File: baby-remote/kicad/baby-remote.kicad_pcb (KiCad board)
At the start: 2 copper layers, 80 x 102 mm, 17 parts, among them SW1 Breast, SW10 Poop, SW11 Both, SW12 Change, SW13 Tummy, SW14 Weight, SW15 Note, SW2 Bottle, SW3 Solid, SW4 Sleep, SW5 PumpL, SW6 PumpR, SW7 Bath, SW8 Meds, SW9 Pee, U1 ESP32-C3 SuperMini

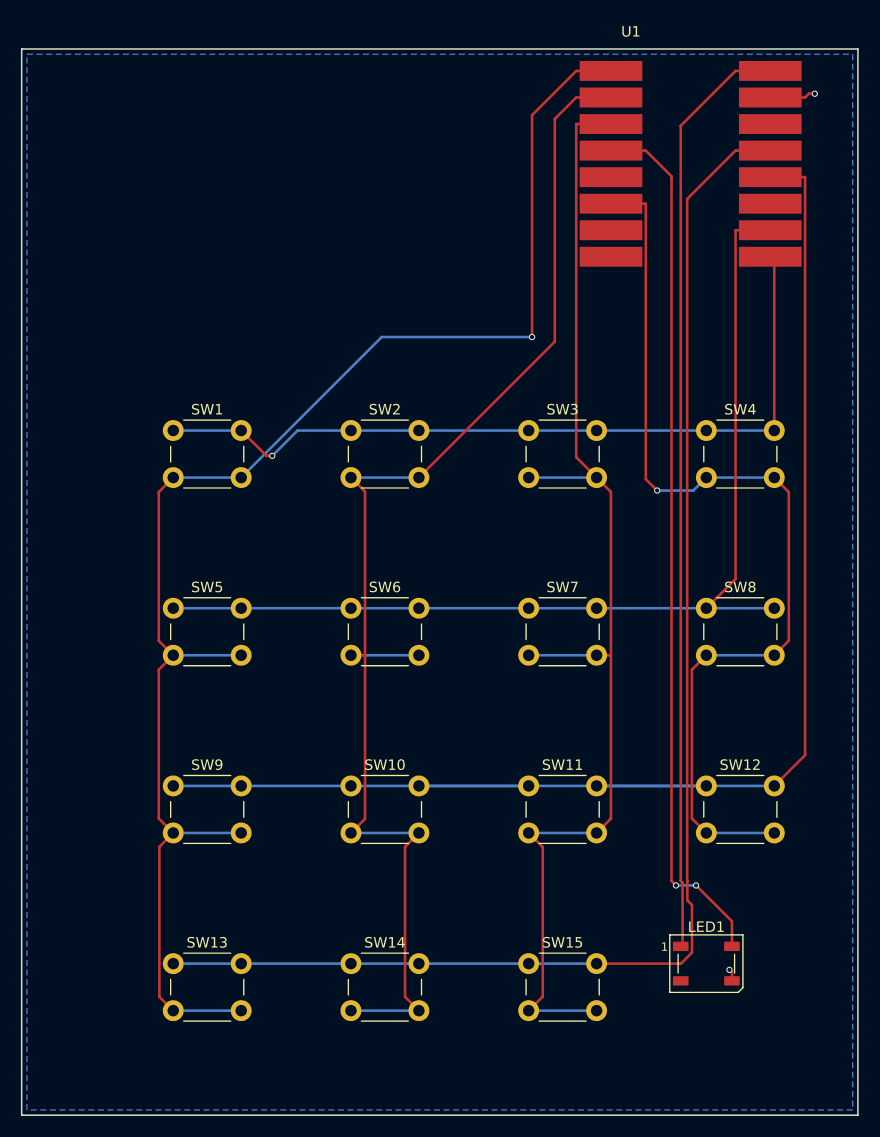
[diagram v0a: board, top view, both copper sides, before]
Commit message: feat(baby-remote): JLCPCB fab package + PCB-carrier enclosure + reserve page
- PCB trimmed to 80x100mm (bottom margin) to hit JLCPCB's <=100x100 5-pc tier;
  DRC still 0/0/0. Gerbers + drill exported to baby-remote/kicad/fab/ (JLCPCB zip).
- Enclosure reworked as a PCB carrier for the manufactured board: 80x100 board
  on a perimeter ledge, snap-fit cover, plunger-in-barrel barrels now hang from
  the cover over board-mounted switches, USB-C opening at the C3 port. STLs
  regenerated. v1 is USB-powered (LiPo deferred to v2).
- README: link the Baby Tracker App (hms-homelab/hms-baby-tracker), fix the STL
  table, add a "Want one?" reserve callout. RESERVE.md points at the
  shmaestro.com waitlist (build-on-demand).

Co-Authored-By: Claude Opus 4.8 (1M context) <noreply@anthropic.com>
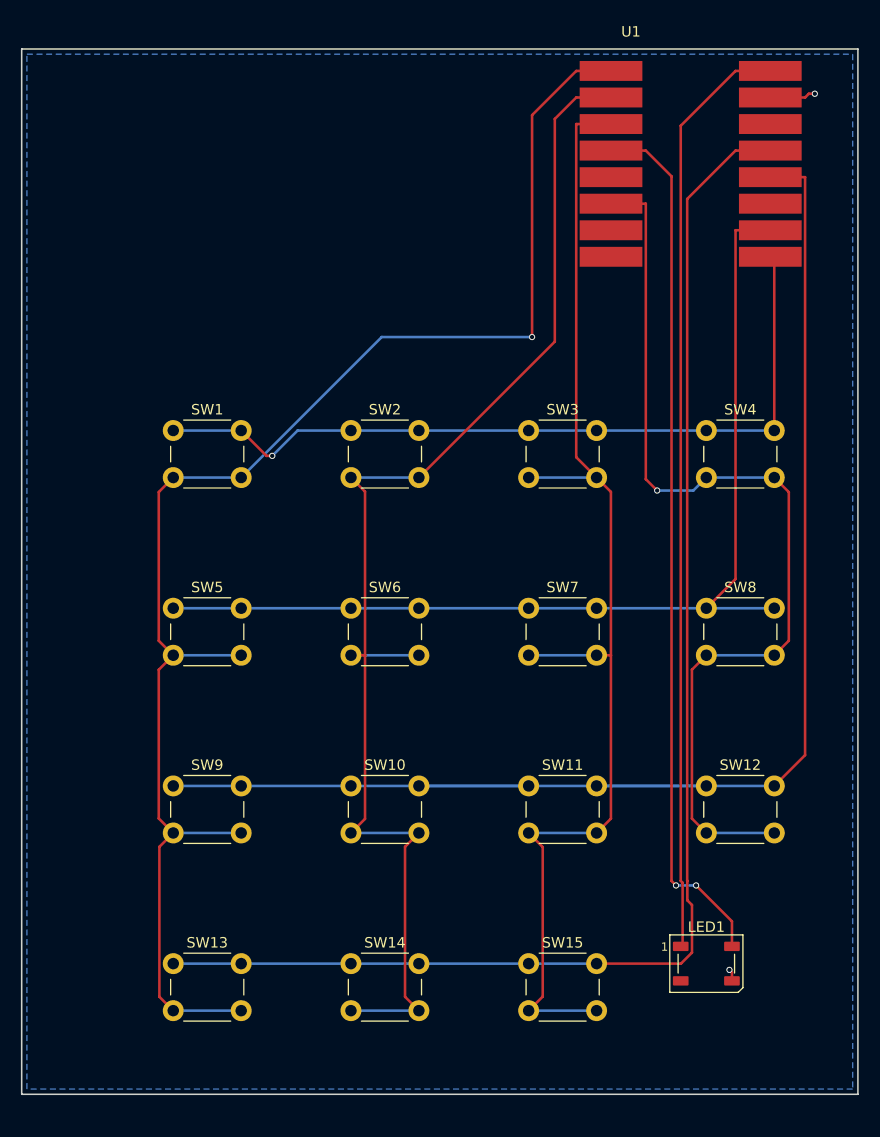
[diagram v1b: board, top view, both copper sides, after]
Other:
- board size 80 x 102 mm -> 80 x 100 mm
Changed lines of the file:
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@@
 	)
 	(gr_line
-		(start 2 104)
+		(start 2 102)
 		(end 2 2)
 		(stroke
@@
 	(gr_line
 		(start 82 2)
-		(end 82 104)
+		(end 82 102)
 		(stroke
 			(width 0.15)
@@
 	)
 	(gr_line
-		(start 82 104)
-		(end 2 104)
+		(start 82 102)
+		(end 2 102)
 		(stroke
 			(width 0.15)
@@
 		(polygon
 			(pts
-				(xy 2.5 2.5) (xy 81.5 2.5) (xy 81.5 103.5) (xy 2.5 103.5)
+				(xy 2.5 2.5) (xy 81.5 2.5) (xy 81.5 101.5) (xy 2.5 101.5)
 			)
 		)
